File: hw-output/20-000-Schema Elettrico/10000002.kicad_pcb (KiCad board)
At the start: 4 copper layers, 45.7 x 32 mm, 29 parts, among them P1 CONN_4, P2 CONN_4, P3 CONN_4, P4 CONN_4, P5 CONN_4, P6 CONN_4, P7 CONN_4, P8 CONN_4, U1 PCF8574, U2 AQZ204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

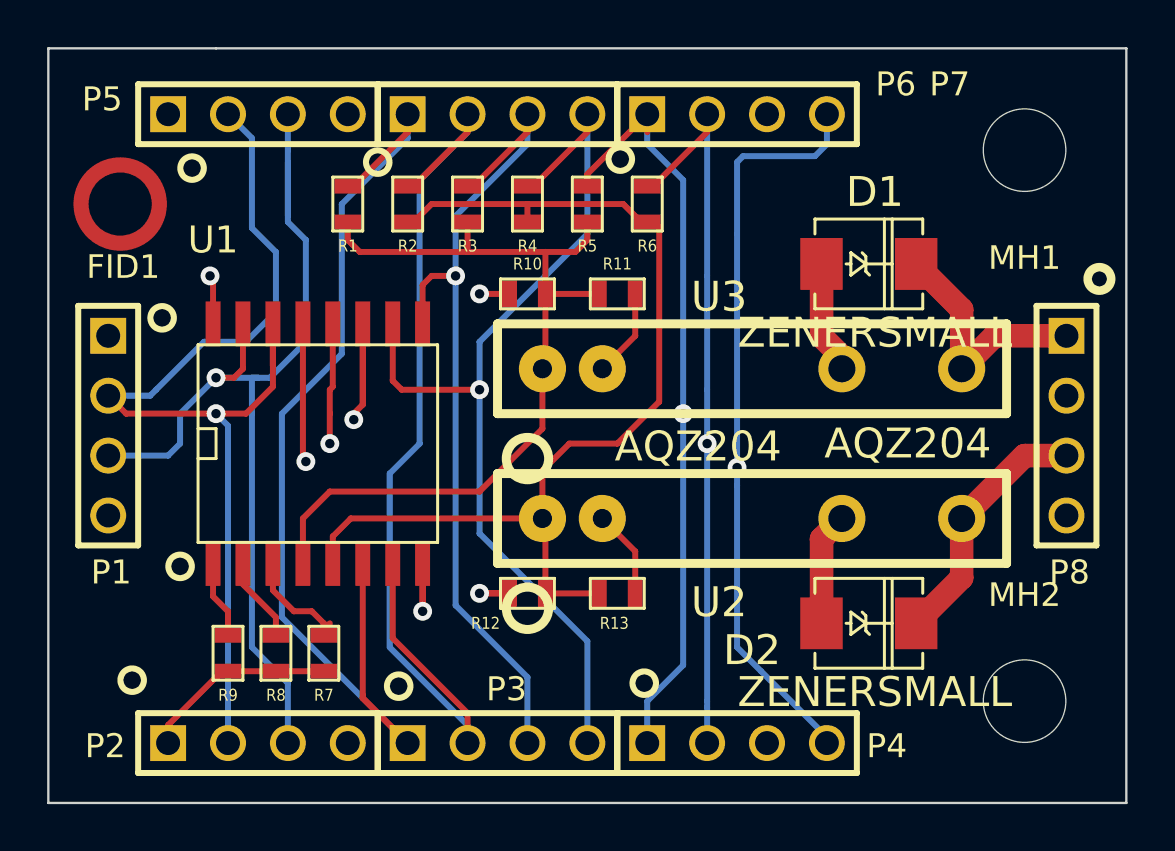
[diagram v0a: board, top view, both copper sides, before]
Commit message: Aggiunte capacità di bypass su alimentazione I2C expander
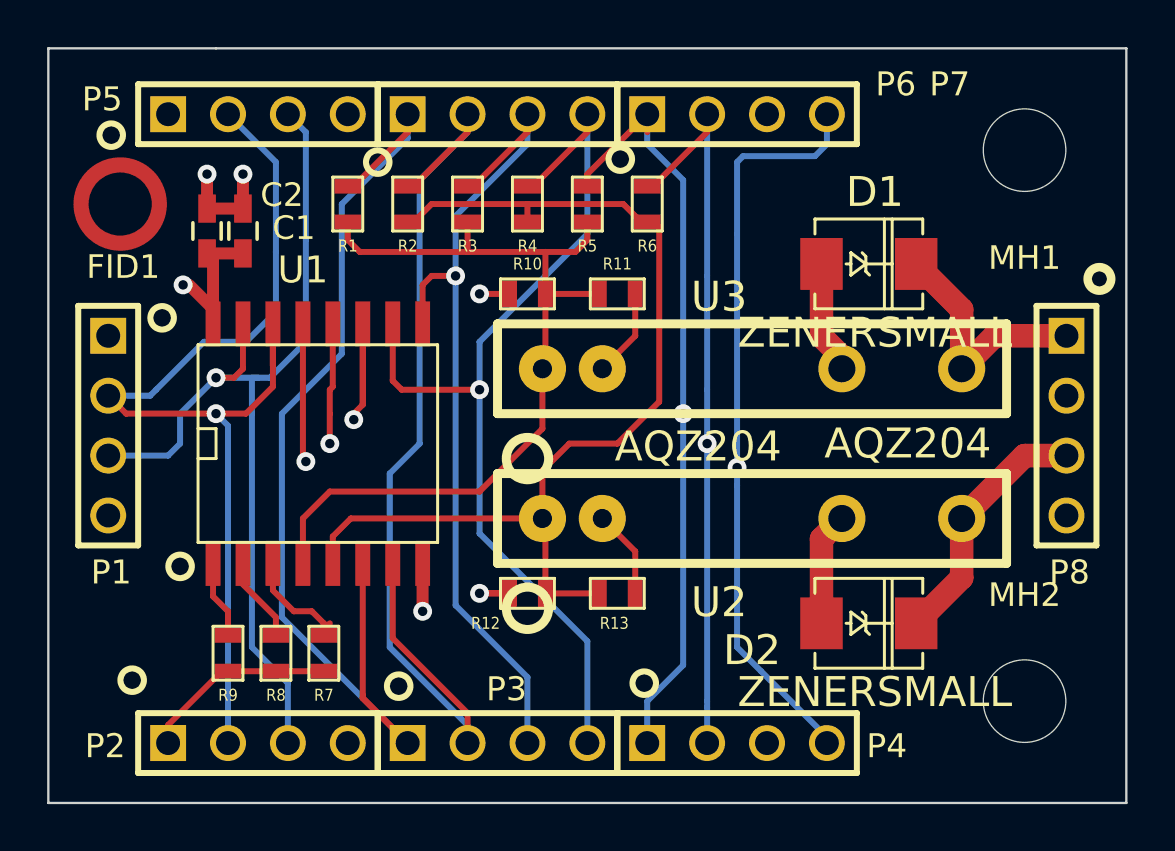
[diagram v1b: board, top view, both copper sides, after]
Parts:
- added C1: 100n, Capacitors_SMD:C_0603_HandSoldering, F.Cu at (92.1, 50.7)
- added C2: 1u, Capacitors_SMD:C_0603_HandSoldering, F.Cu at (90.6, 50.7)
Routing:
- net VDD: track 14.2 -> 19.2 mm
- net GND: track 11.6 -> 16.0 mm, vias 1 -> 3
- net /I2C_SDA: track 43.0 -> 40.7 mm
